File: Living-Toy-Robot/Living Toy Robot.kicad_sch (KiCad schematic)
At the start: 15 parts, among them J1 REGULATED 5V / 3A SUPPLY, M1 SG90 / approx 70 deg travel, SW1 COPPER-TAPE DOOR, U1 Adafruit CPX / PID 3333, U2 Adafruit STEMMA / PID 3885

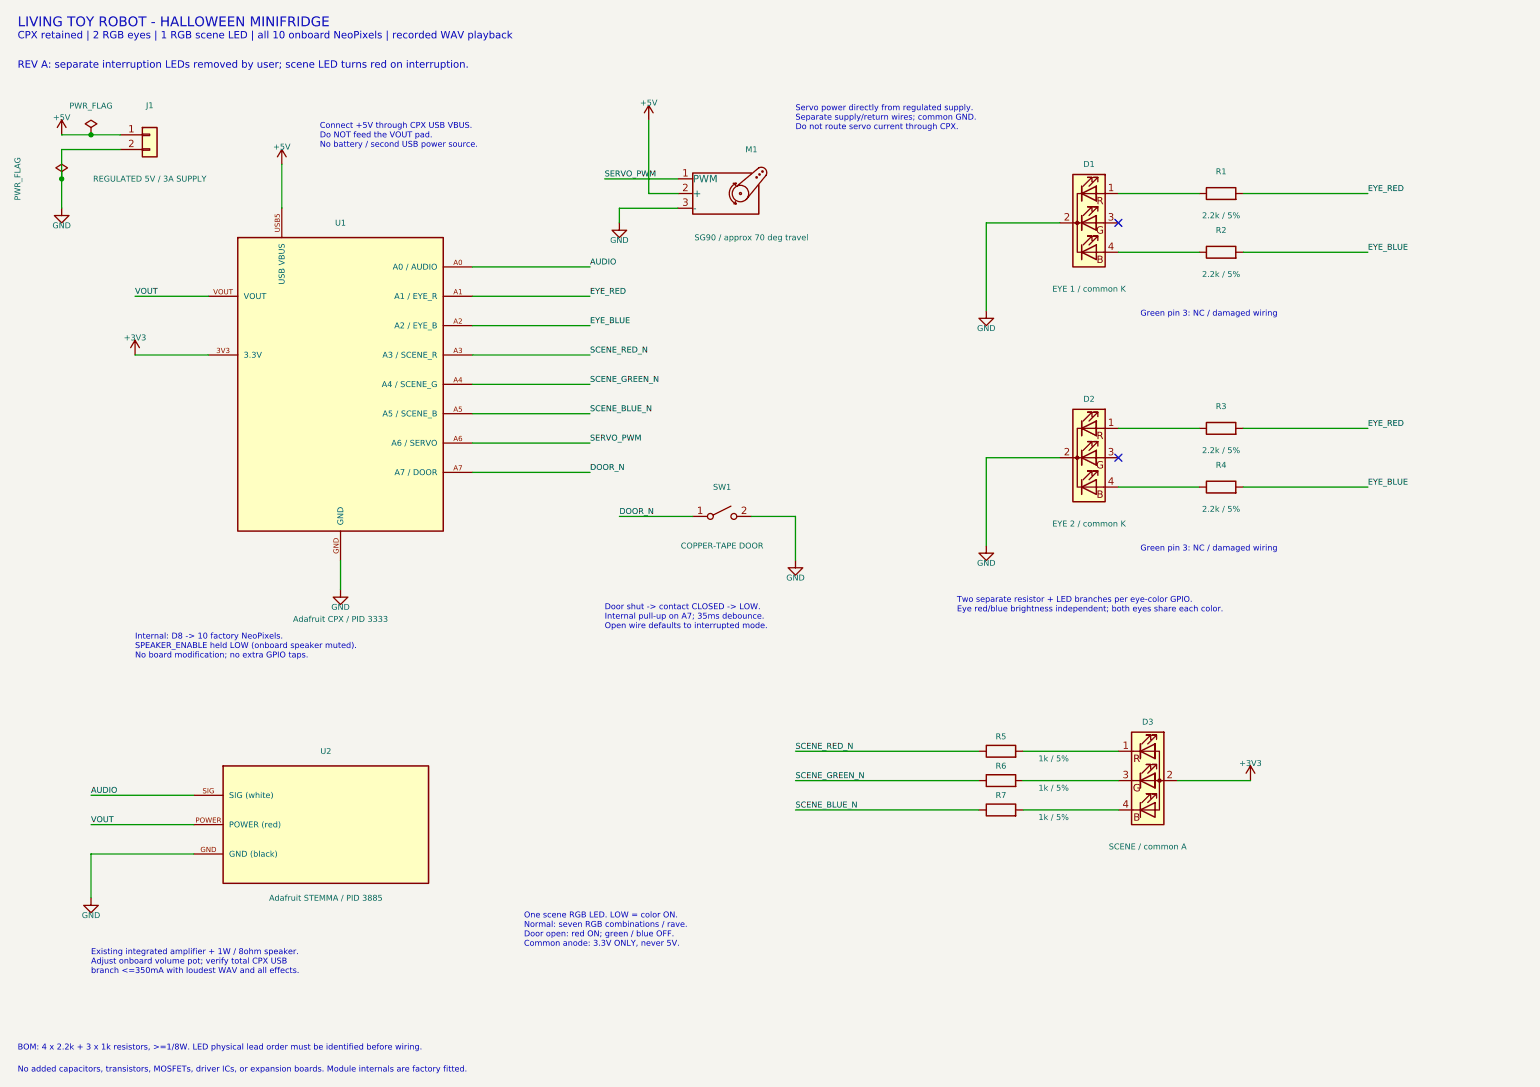
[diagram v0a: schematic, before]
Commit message: Use three parallel scene RGB LEDs with individually limited GPIO current (revision B)
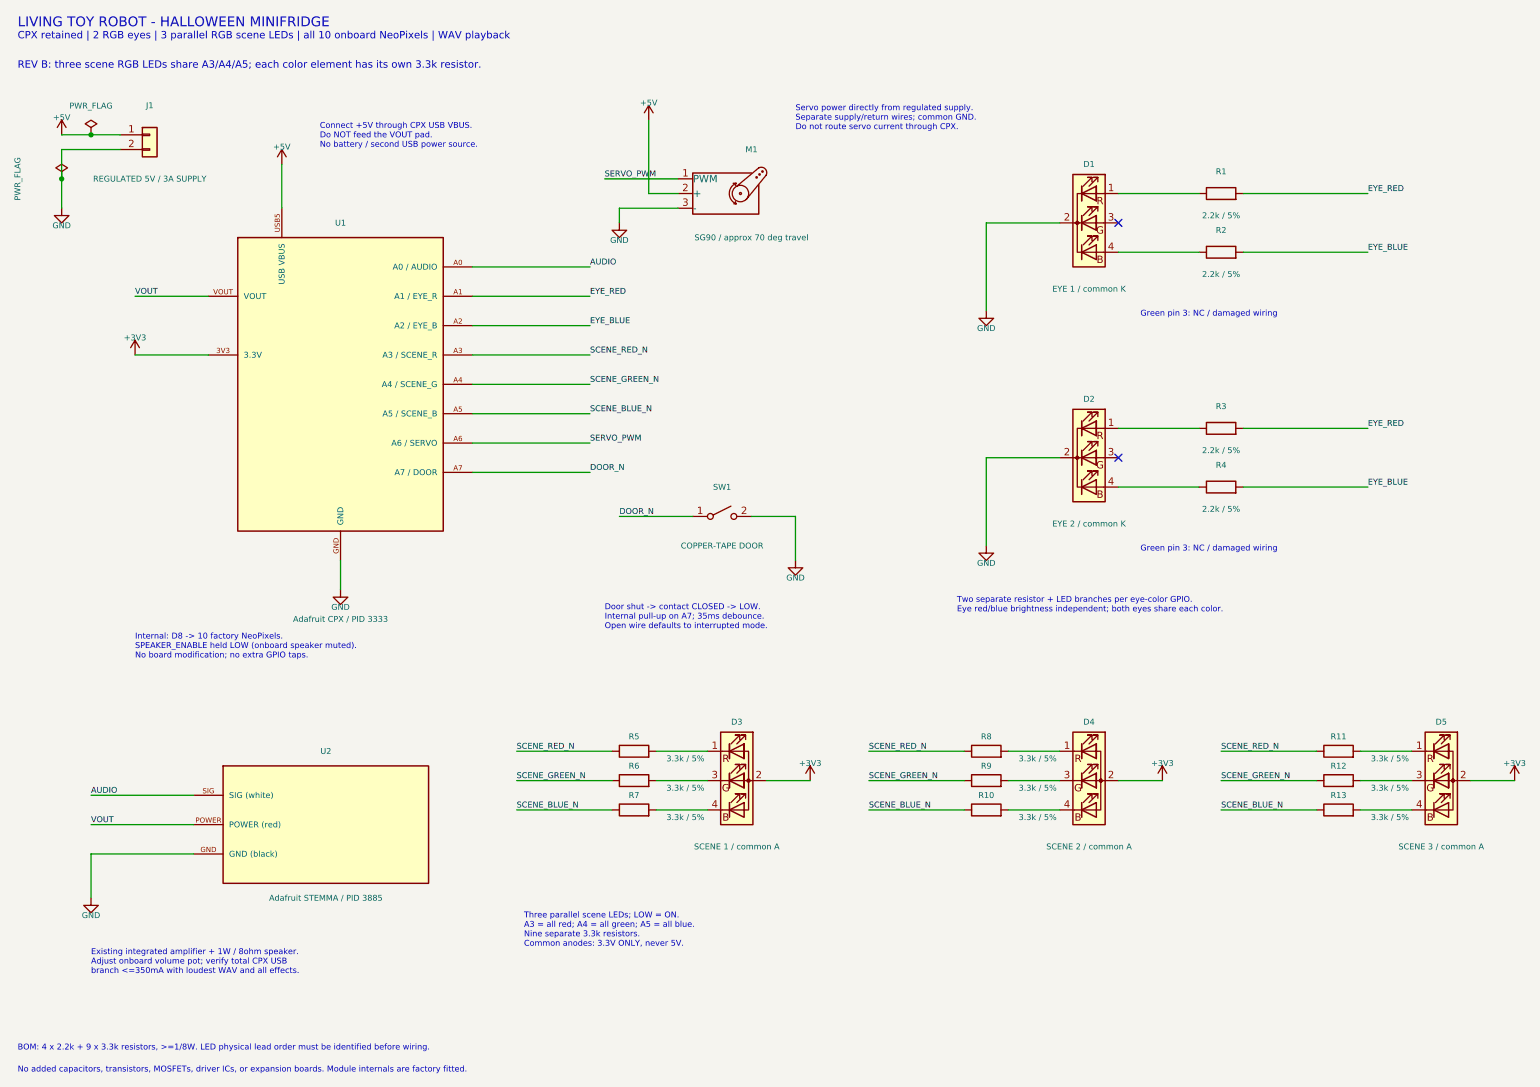
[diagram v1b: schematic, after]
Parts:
- added D4: SCENE 2 / common A, symbol Device:LED_RAGB
- added D5: SCENE 3 / common A, symbol Device:LED_RAGB
- added R10, R11, R12, R13, R8, R9: 3.3k / 5%, symbol Device:R
- D3: value SCENE / common A -> SCENE 1 / common A
- R5, R6, R7: value 1k / 5% -> 3.3k / 5%
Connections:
- net +3V3: now also D4.2 (A), D5.2 (A)
- net SCENE_BLUE_N: now also R10.1, R13.1
- net SCENE_GREEN_N: now also R12.1, R9.1
- net SCENE_RED_N: now also R11.1, R8.1
- new net: D5.4 (BK), R13.2
- new net: D4.3 (GK), R9.2
- new net: D4.4 (BK), R10.2
- new net: D5.1 (RK), R11.2
- new net: D4.1 (RK), R8.2
- new net: D5.3 (GK), R12.2
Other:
- note added: "BOM: 4 x 2.2k + 9 x 3.3k resistors, >=1/8W. LED physical lead order must be identified before wiring."
- note added: "CPX retained | 2 RGB eyes | 3 parallel RGB scene LEDs | all 10 onboard NeoPixels | WAV playback"
- note added: "REV B: three scene RGB LEDs share A3/A4/A5; each color element has its own 3.3k resistor."
- note added: "Three parallel scene LEDs; LOW = ON. A3 = all red; A4 = all green; A5 = all blue. Nine separate 3.3k resistors. Common anodes: 3.3V ONLY, never 5V."
- note removed: "BOM: 4 x 2.2k + 3 x 1k resistors, >=1/8W. LED physical lead order must be identified before wiring."
- note removed: "CPX retained | 2 RGB eyes | 1 RGB scene LED | all 10 onboard NeoPixels | recorded WAV playback"
- note removed: "One scene RGB LED. LOW = color ON. Normal: seven RGB combinations / rave. Door open: red ON; green / blue OFF. Common anode: 3.3V ONLY, never 5V."
- note removed: "REV A: separate interruption LEDs removed by user; scene LED turns red on interruption."

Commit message: Use two scene RGB LEDs with six individual 2.2k resistors (revision C)
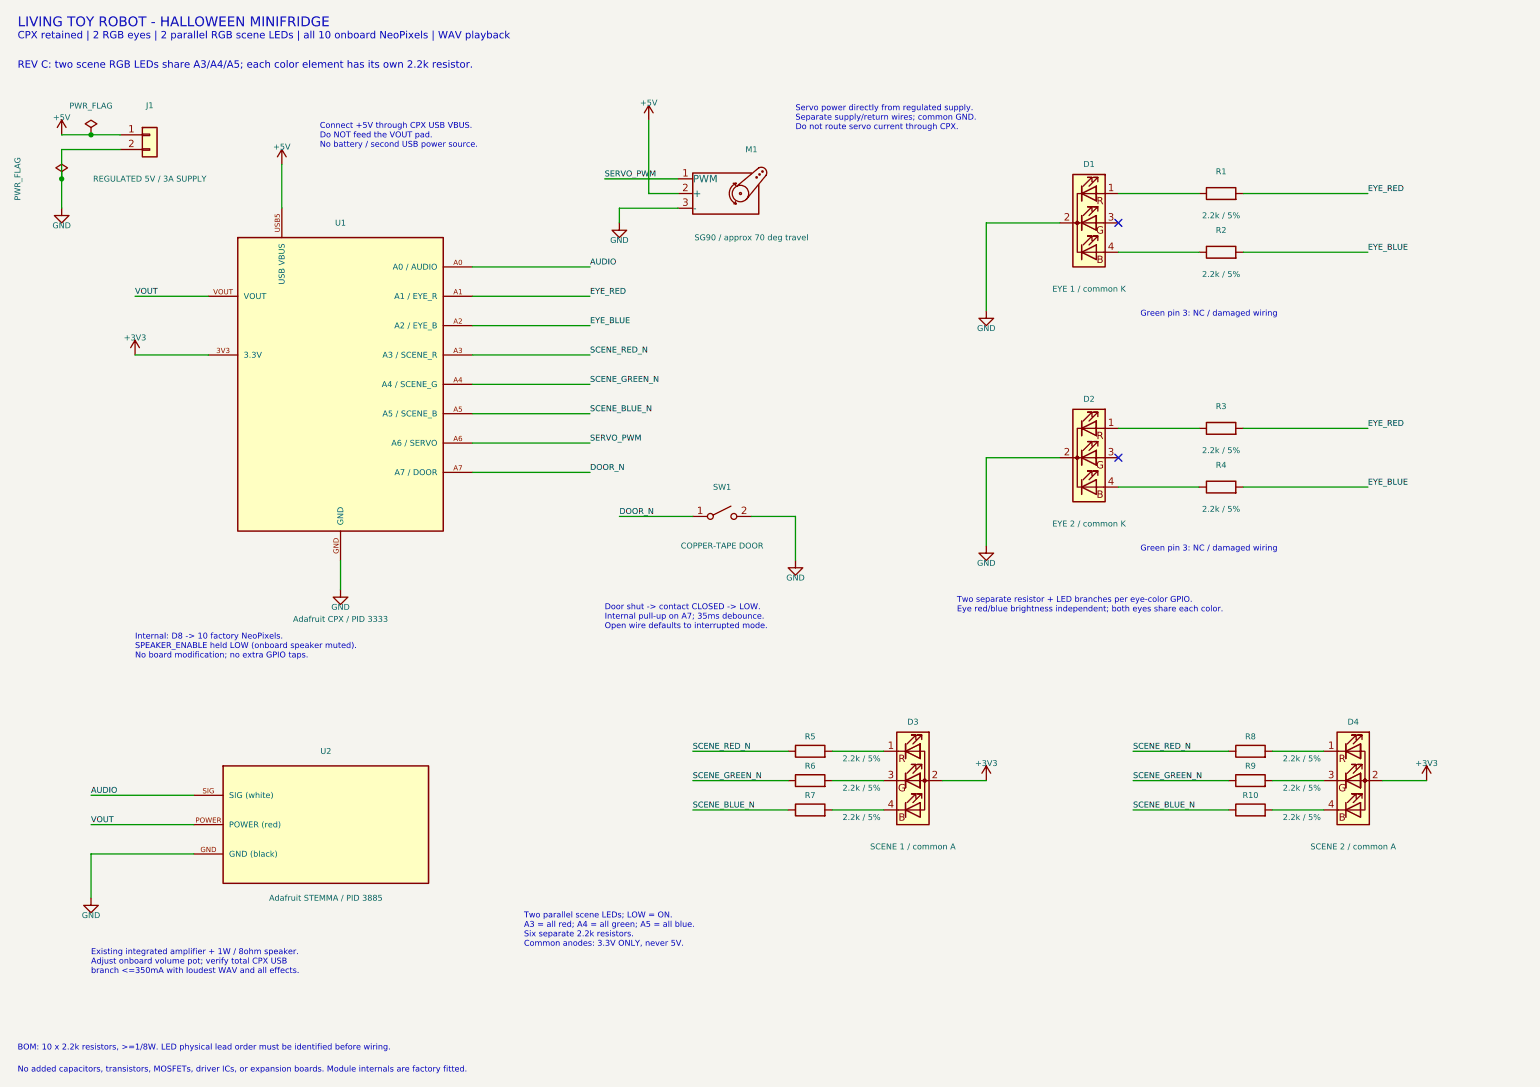
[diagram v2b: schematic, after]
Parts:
- removed D5: SCENE 3 / common A, symbol Device:LED_RAGB
- removed R11, R12, R13: 3.3k / 5%, symbol Device:R
- R10, R5, R6, R7, R8, R9: value 3.3k / 5% -> 2.2k / 5%
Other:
- note added: "BOM: 10 x 2.2k resistors, >=1/8W. LED physical lead order must be identified before wiring."
- note added: "CPX retained | 2 RGB eyes | 2 parallel RGB scene LEDs | all 10 onboard NeoPixels | WAV playback"
- note added: "REV C: two scene RGB LEDs share A3/A4/A5; each color element has its own 2.2k resistor."
- note added: "Two parallel scene LEDs; LOW = ON. A3 = all red; A4 = all green; A5 = all blue. Six separate 2.2k resistors. Common anodes: 3.3V ONLY, never 5V."
- note removed: "BOM: 4 x 2.2k + 9 x 3.3k resistors, >=1/8W. LED physical lead order must be identified before wiring."
- note removed: "CPX retained | 2 RGB eyes | 3 parallel RGB scene LEDs | all 10 onboard NeoPixels | WAV playback"
- note removed: "REV B: three scene RGB LEDs share A3/A4/A5; each color element has its own 3.3k resistor."
- note removed: "Three parallel scene LEDs; LOW = ON. A3 = all red; A4 = all green; A5 = all blue. Nine separate 3.3k resistors. Common anodes: 3.3V ONLY, never 5V."
